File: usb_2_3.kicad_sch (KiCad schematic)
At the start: 21 parts, among them J4 USB3_A_Stacked, J4B USB3_A_Stacked, J5 USB_A_Stacked, U3 D3V3XA4B10LP, U4 D3V3XA4B10LP, U5 D3V3XA4B10LP

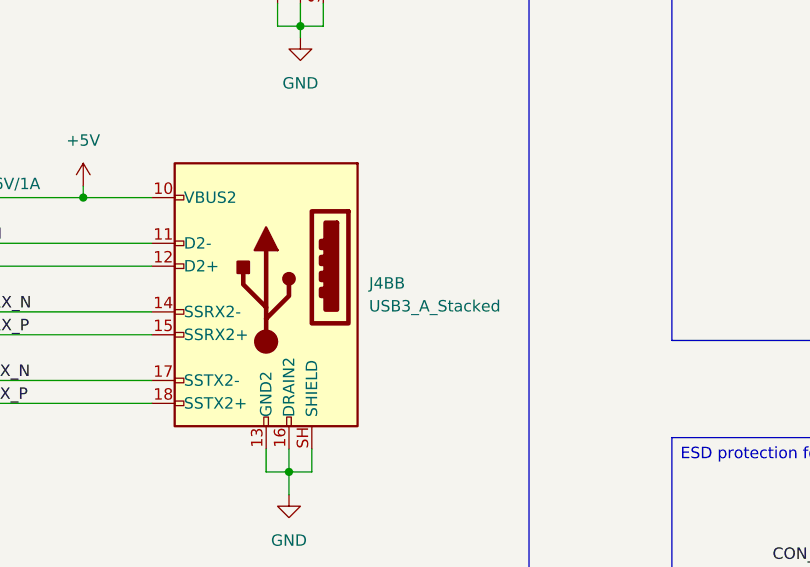
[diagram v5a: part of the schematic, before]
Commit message: finished the entire schematic capture for each of the sub sheets .and then the next part is to .fix all the erc errors when impoting the shematic in to the pcb to get readu for routing
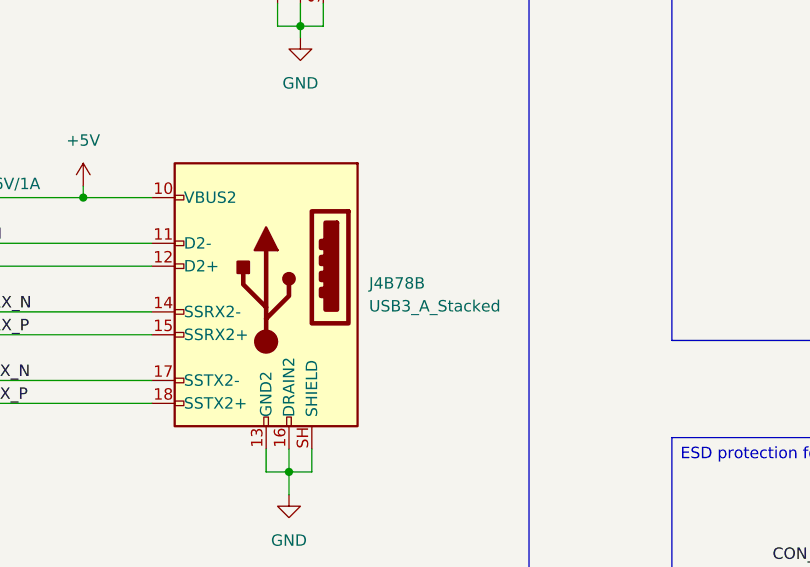
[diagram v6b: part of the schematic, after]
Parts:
- renumbered J4B to J4B78
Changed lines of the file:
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@@
 		(dnp no)
 		(fields_autoplaced yes)
-		(property "Reference" "J4B"
+		(property "Reference" "J4B78"
 			(at 111.76 88.2649 0)
 			(show_name no)
@@
 			(project "Carrier_Board"
 				(path "/e768274e-12f3-4f83-96f6-abb7638e0bc1/f6805346-90aa-47cf-a186-fe5806ffb5a5"
-					(reference "J4B")
+					(reference "J4B78")
 					(unit 2)
 				)

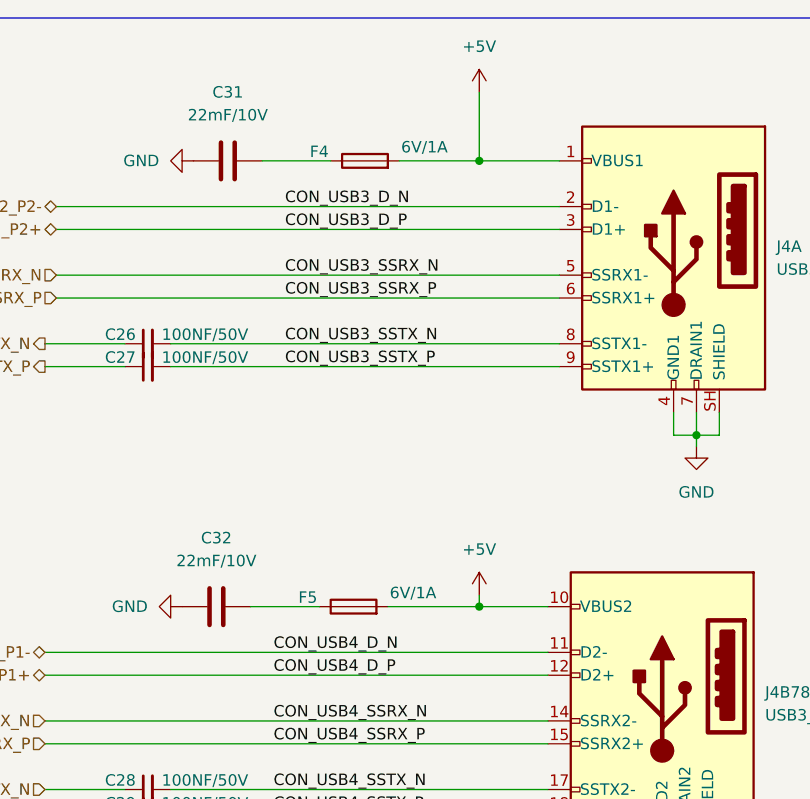
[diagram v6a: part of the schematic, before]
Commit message: Fixed annotation errors duplicate designators on passive components R11 and J15 so that schematic could be imported into pcb. There might be some missing footprints... starting that investigation
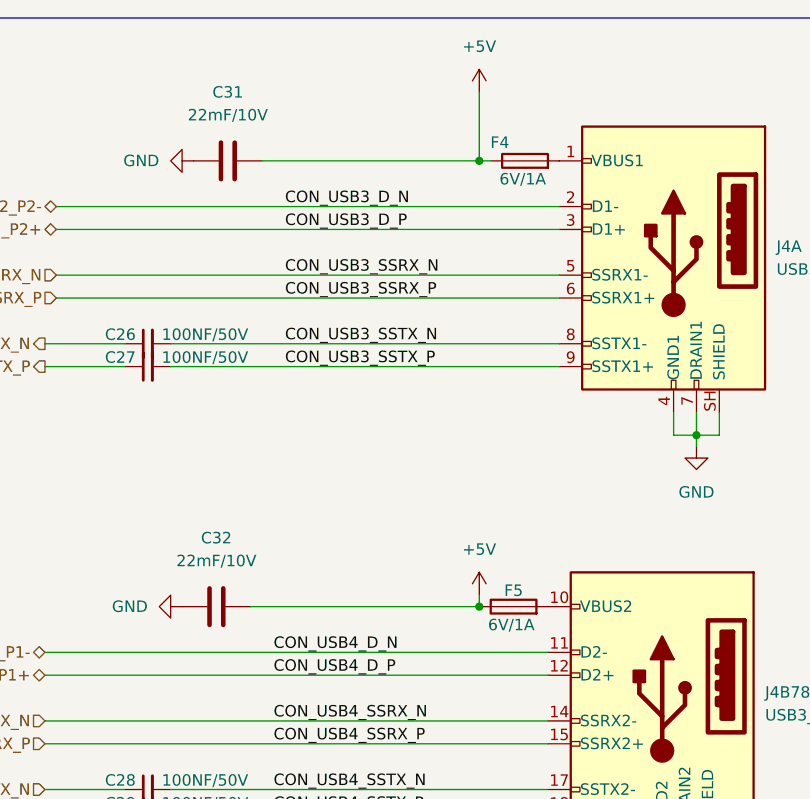
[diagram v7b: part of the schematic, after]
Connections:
- net +5V: now also C31.2, C32.2, F4.1, F5.1; no longer F4.2, F5.2, J4.1 (VBUS1), J4B78.10 (VBUS2)
- new net: F5.2, J4B78.10 (VBUS2)
- new net: F4.2, J4.1 (VBUS1)
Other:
- moved on the sheet: F4, F5
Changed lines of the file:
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@@
 	)
 	(junction
-		(at 237.49 67.31)
+		(at 80.01 29.21)
 		(diameter 0)
 		(color 0 0 0 0)
 	)
 	(junction
-		(at 210.82 129.54)
+		(at 237.49 67.31)
 		(diameter 0)
 		(color 0 0 0 0)
 	)
 	(junction
-		(at 80.01 29.21)
+		(at 210.82 129.54)
 		(diameter 0)
 		(color 0 0 0 0)
@@
 	(wire
 		(pts
+			(xy 80.01 29.21) (xy 81.28 29.21)
+		)
+		(stroke
+			(width 0)
+			(type default)
+		)
+	)
+	(wire
+		(pts
 			(xy 170.18 129.54) (xy 186.69 129.54)
 		)
@@
 	(wire
 		(pts
-			(xy 55.88 29.21) (xy 63.5 29.21)
+			(xy 55.88 29.21) (xy 80.01 29.21)
 		)
 		(stroke
@@
 	(wire
 		(pts
-			(xy 71.12 29.21) (xy 80.01 29.21)
+			(xy 100.33 106.68) (xy 100.33 109.22)
 		)
 		(stroke
@@
 	(wire
 		(pts
-			(xy 100.33 106.68) (xy 100.33 109.22)
+			(xy 33.02 44.45) (xy 88.9 44.45)
 		)
 		(stroke
@@
 	(wire
 		(pts
-			(xy 33.02 44.45) (xy 88.9 44.45)
+			(xy 54.61 78.74) (xy 80.01 78.74)
 		)
 		(stroke
@@
 	(wire
 		(pts
-			(xy 80.01 78.74) (xy 87.63 78.74)
-		)
-		(stroke
-			(width 0)
-			(type default)
-		)
-	)
-	(wire
-		(pts
 			(xy 80.01 21.59) (xy 80.01 29.21)
 		)
@@
 	(wire
 		(pts
-			(xy 69.85 78.74) (xy 80.01 78.74)
-		)
-		(stroke
-			(width 0)
-			(type default)
-		)
-	)
-	(wire
-		(pts
 			(xy 170.18 119.38) (xy 186.69 119.38)
 		)
@@
 		)
 	)
-	(wire
-		(pts
-			(xy 80.01 29.21) (xy 88.9 29.21)
-		)
-		(stroke
-			(width 0)
-			(type default)
-		)
-	)
-	(wire
-		(pts
-			(xy 54.61 78.74) (xy 62.23 78.74)
-		)
-		(stroke
-			(width 0)
-			(type default)
-		)
-	)
 	(label "CON_USB3_SSRX_P"
 		(at 58.42 44.45 0)
@@
 	(symbol
 		(lib_id "Device:Fuse")
-		(at 66.04 78.74 90)
+		(at 83.82 78.74 90)
 		(unit 1)
 		(body_style 1)
@@
 		(dnp no)
 		(property "Reference" "F5"
-			(at 60.96 77.724 90)
+			(at 83.82 76.962 90)
 			(show_name no)
 			(do_not_autoplace no)
@@
 		)
 		(property "Value" "6V/1A"
-			(at 72.644 77.216 90)
+			(at 83.566 80.772 90)
 			(show_name no)
 			(do_not_autoplace no)
@@
 		)
 		(property "Footprint" "A_HDJ_Library:Fuse_0805_2012Metric"
-			(at 66.04 80.518 90)
+			(at 83.82 80.518 90)
 			(hide yes)
 			(show_name no)
@@
 		)
 		(property "Datasheet" ""
-			(at 66.04 78.74 0)
+			(at 83.82 78.74 0)
 			(hide yes)
 			(show_name no)
@@
 		)
 		(property "Description" "Fuse"
-			(at 66.04 78.74 0)
+			(at 83.82 78.74 0)
 			(hide yes)
 			(show_name no)
@@
 		)
 		(property "Purpose" ""
-			(at 66.04 78.74 0)
+			(at 83.82 78.74 0)
 			(show_name no)
 			(do_not_autoplace no)
@@
 	(symbol
 		(lib_id "Device:Fuse")
-		(at 67.31 29.21 90)
+		(at 85.09 29.21 90)
 		(unit 1)
 		(body_style 1)
@@
 		(dnp no)
 		(property "Reference" "F4"
-			(at 62.23 28.194 90)
+			(at 82.296 27.178 90)
 			(show_name no)
 			(do_not_autoplace no)
@@
 		)
 		(property "Value" "6V/1A"
-			(at 73.914 27.686 90)
+			(at 84.836 31.242 90)
 			(show_name no)
 			(do_not_autoplace no)
@@
 		)
 		(property "Footprint" "A_HDJ_Library:Fuse_0805_2012Metric"
-			(at 67.31 30.988 90)
+			(at 85.09 30.988 90)
 			(hide yes)
 			(show_name no)
@@
 		)
 		(property "Datasheet" ""
-			(at 67.31 29.21 0)
+			(at 85.09 29.21 0)
 			(hide yes)
 			(show_name no)
@@
 		)
 		(property "Description" "Fuse"
-			(at 67.31 29.21 0)
+			(at 85.09 29.21 0)
 			(hide yes)
 			(show_name no)
@@
 		)
 		(property "Purpose" ""
-			(at 67.31 29.21 0)
+			(at 85.09 29.21 0)
 			(show_name no)
 			(do_not_autoplace no)

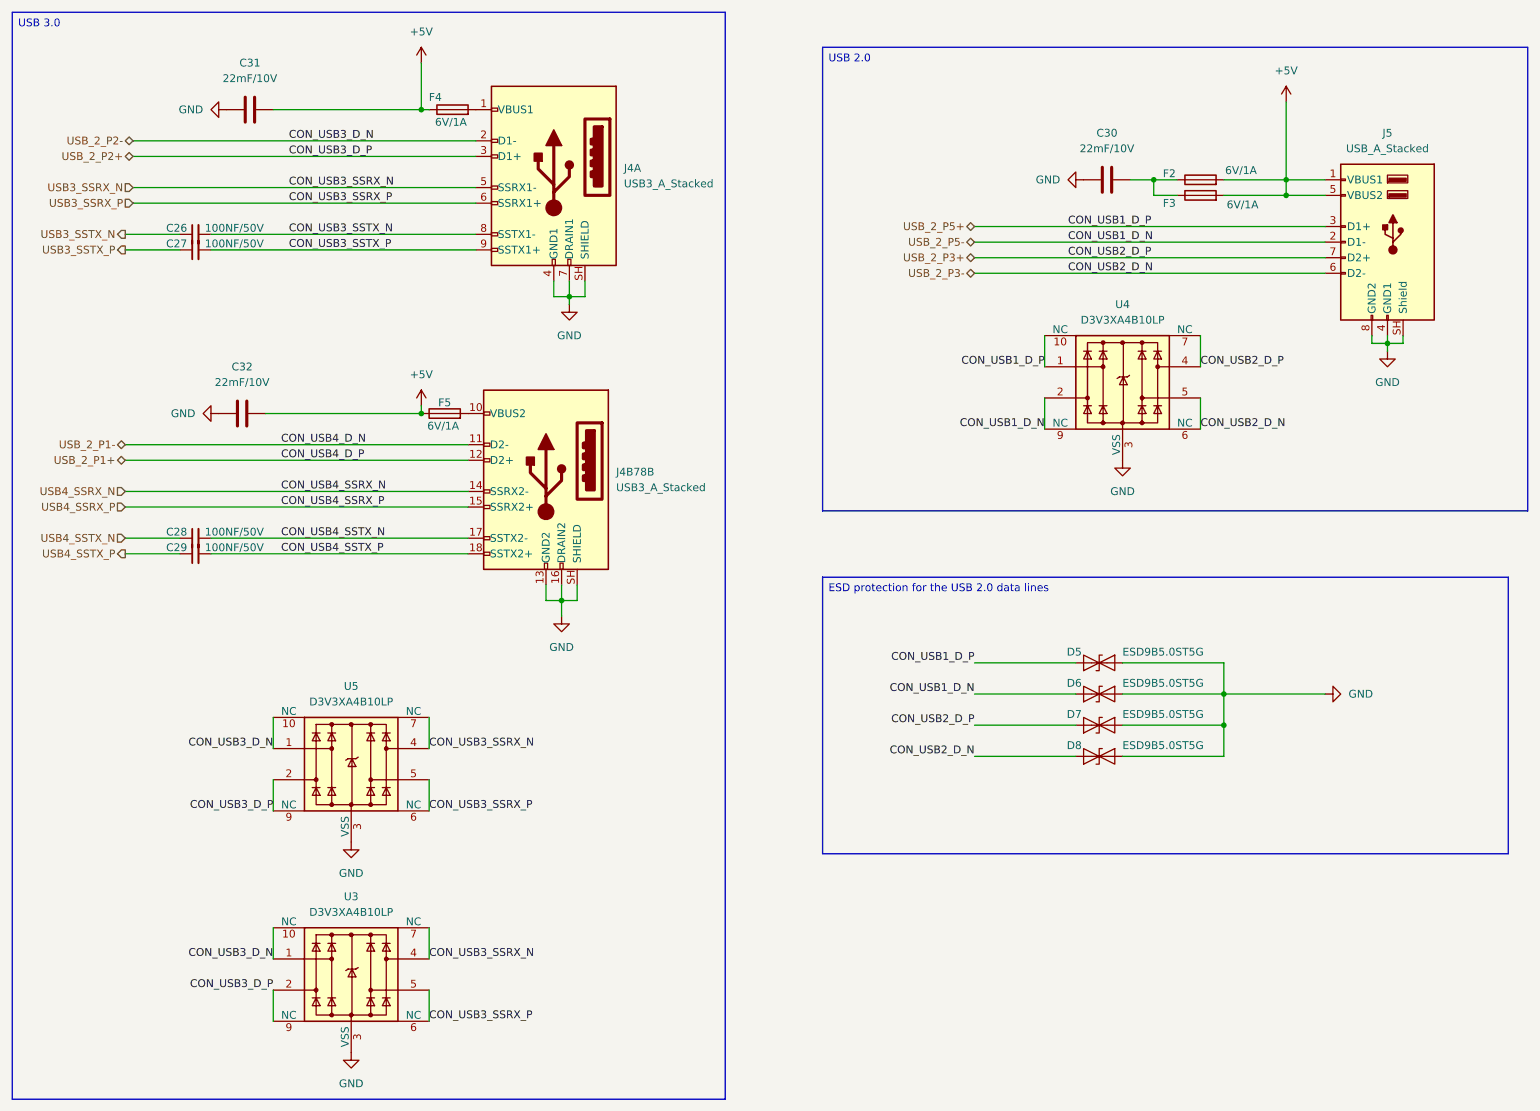
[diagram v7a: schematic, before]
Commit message: Updated all the footprints into the pcb editor but all the designator numbers have changed... I have tp go back and fix each one
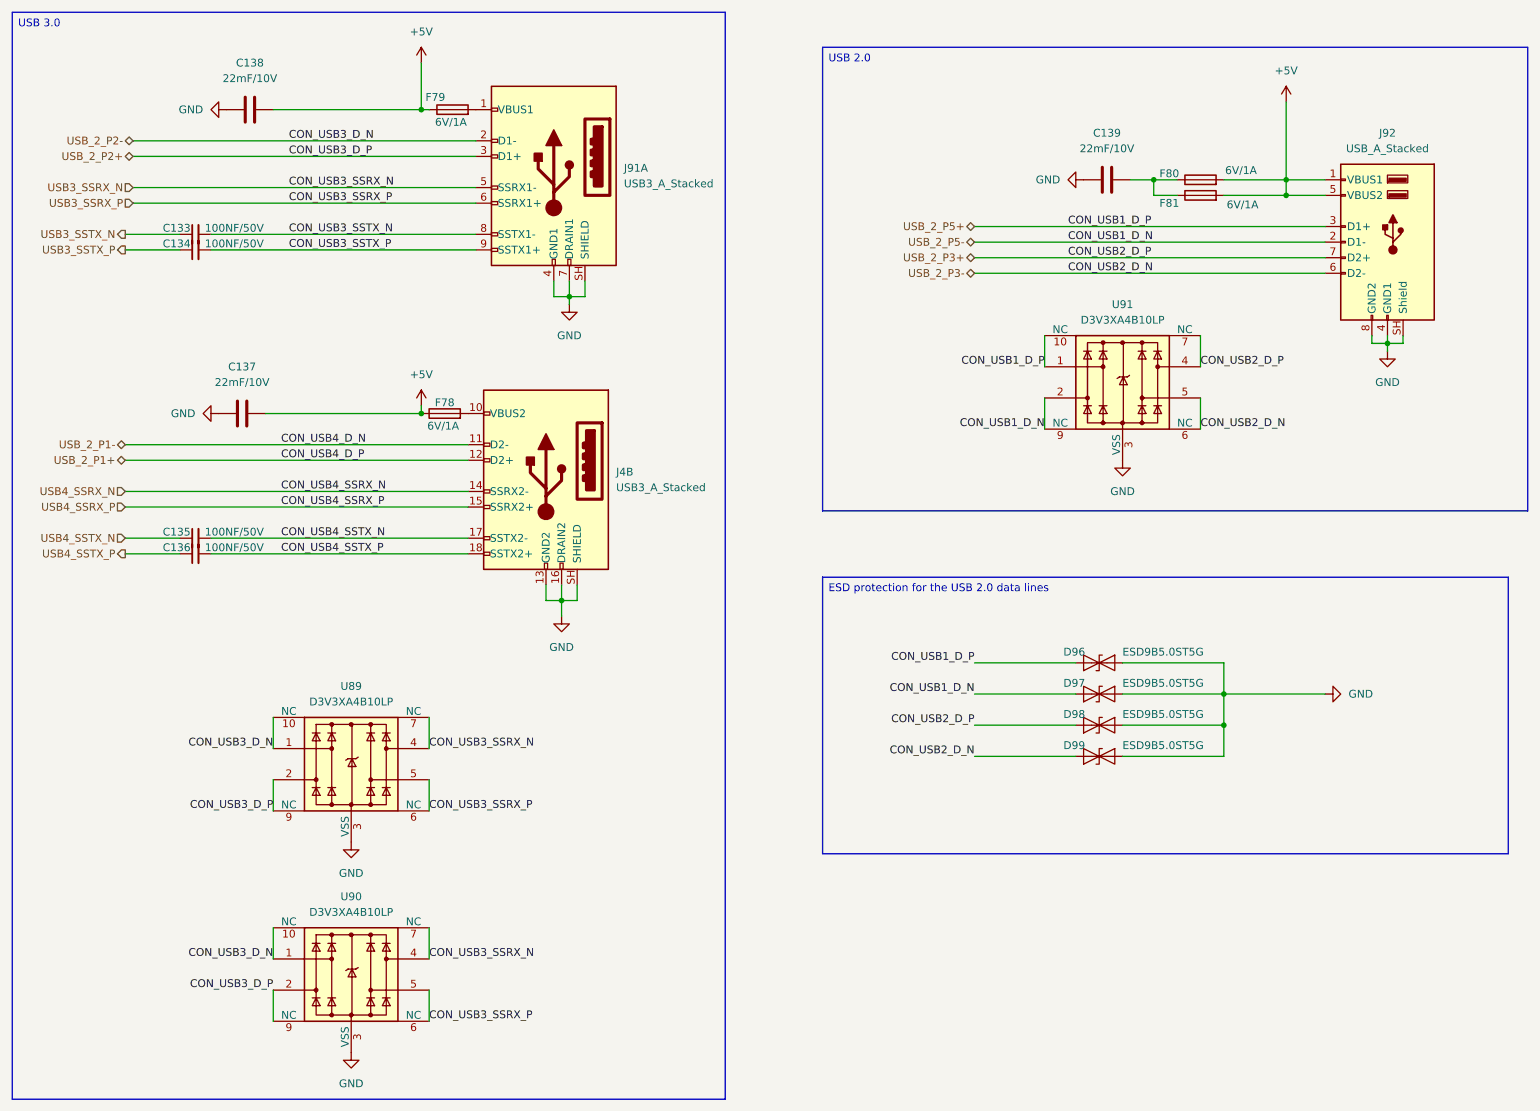
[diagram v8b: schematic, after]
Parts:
- J4: renamed from J4B78; footprint (none) -> A_HDJ_Library:USB3_A_Molex_48406-0001_Horizontal_Stacked
- renumbered C26 to C133, C27 to C134, C28 to C135, C29 to C136, C32 to C137, C31 to C138, C30 to C139, D5 to D96, D6 to D97, D7 to D98, D8 to D99, F5 to F78, F4 to F79, F2 to F80, F3 to F81, J4 to J91, J5 to J92, U5 to U89, U3 to U90, U4 to U91
